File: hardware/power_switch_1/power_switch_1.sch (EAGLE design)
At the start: 21 parts, among them IC1 MEGA168/328, IC2 RFM12, IC3 LP2950Z, K1 FTR-K1C, T1 BC547, X1 SW Out

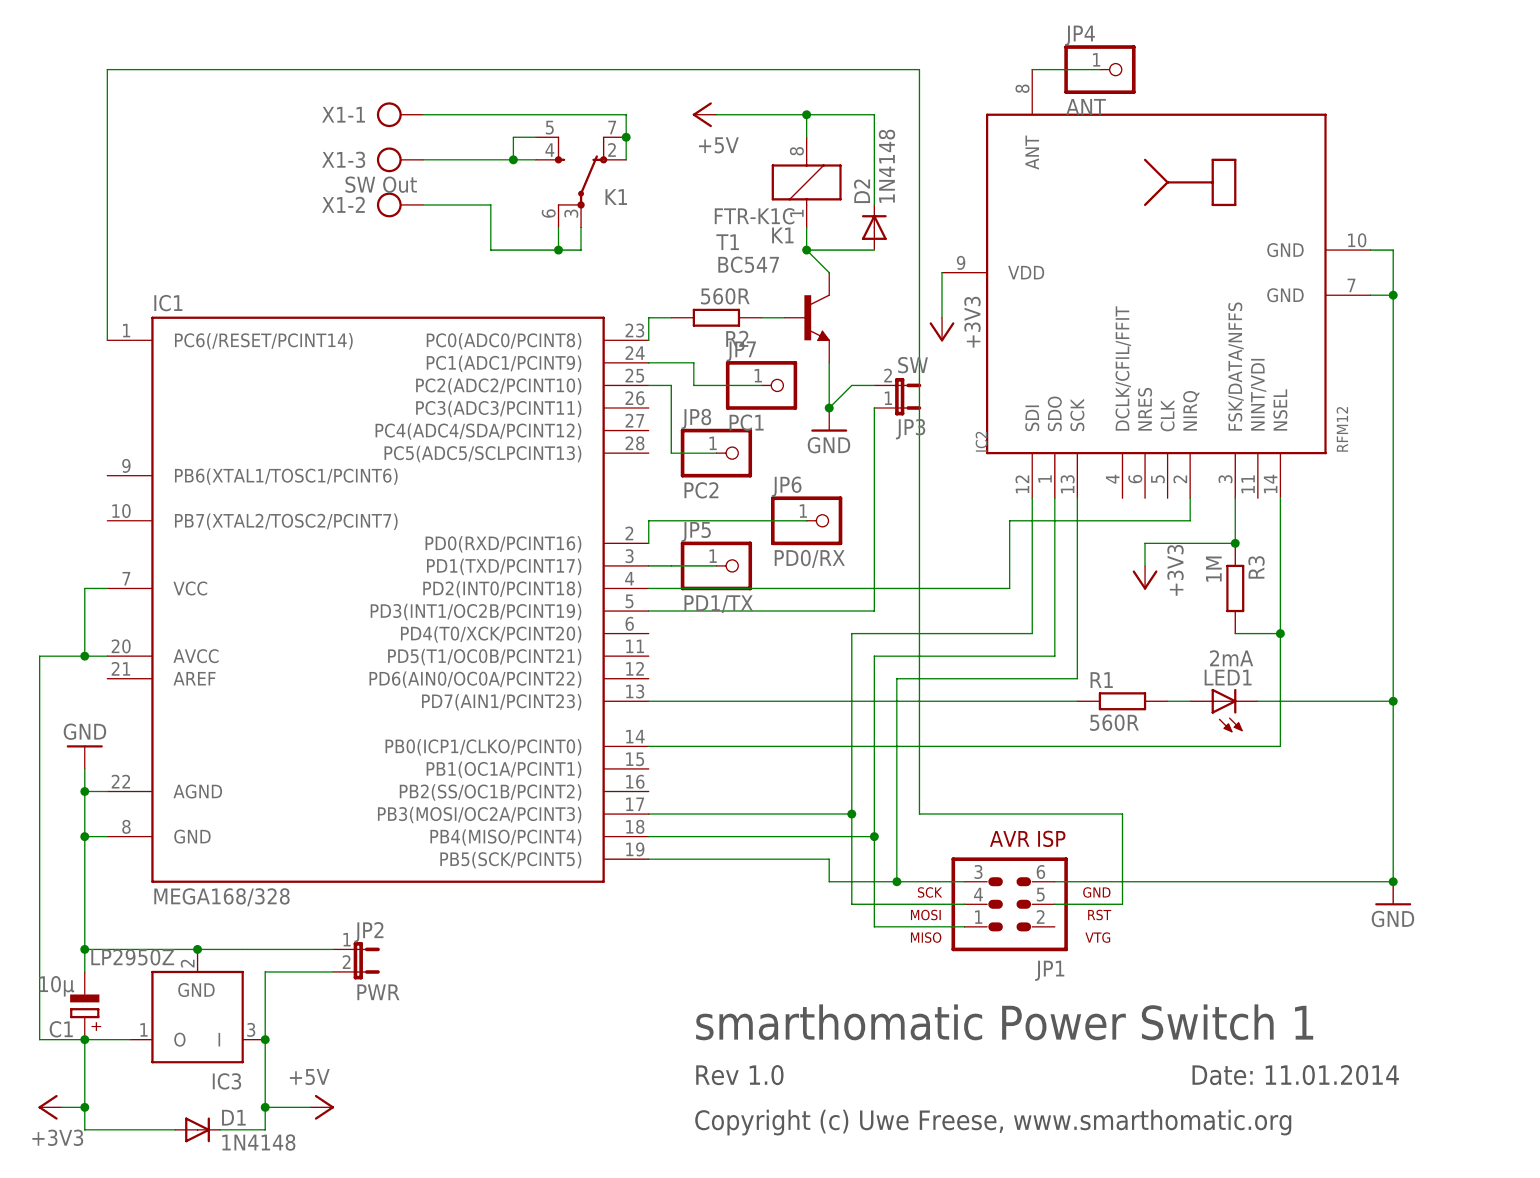
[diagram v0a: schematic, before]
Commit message: In PCB V1.1, the power pin of the RFM module is connected to an ATMega pin to allow restart if needed.
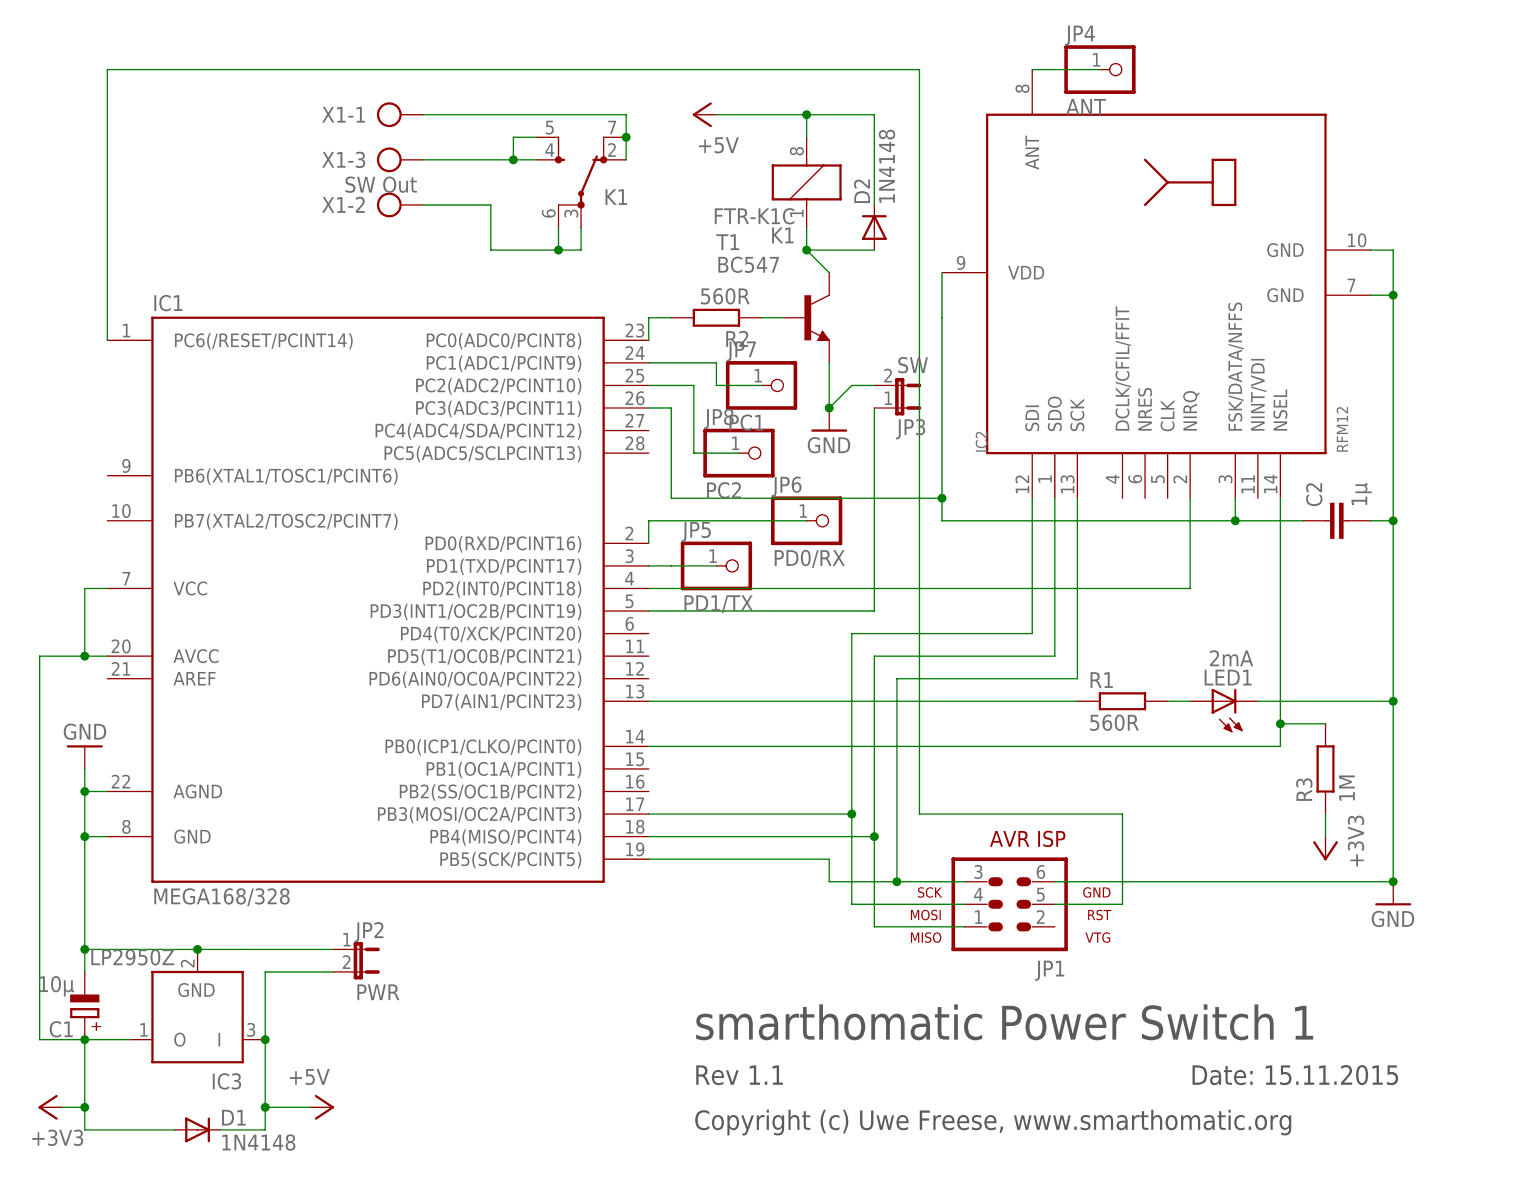
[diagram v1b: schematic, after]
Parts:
- added C2: 1µ, capacitor-wima:C5/3.5
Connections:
- new net N$22: C2.1, IC1.PC3(ADC3/PCINT11), IC2.FSK/DATA/NFFS, IC2.VDD
- net +3V3: no longer IC2.FSK/DATA/NFFS, IC2.VDD
- net GND: now also C2.2
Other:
- note added: "Date: 15.11.2015"
- note added: "Rev 1.1"
- note removed: "Date: 11.01.2014"
- note removed: "Rev 1.0"
- moved on the sheet: JP8, R3
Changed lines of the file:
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@@
 <?xml version="1.0" encoding="utf-8"?>
 <!DOCTYPE eagle SYSTEM "eagle.dtd">
-<eagle version="6.4">
+<eagle version="7.3.0">
 <drawing>
 <settings>
@@
 <part name="P+5" library="supply1" deviceset="+5V" device=""/>
 <part name="T1" library="transistor" deviceset="BC547" device=""/>
-<part name="+3V2" library="supply1" deviceset="+3V3" device=""/>
 <part name="+3V3" library="supply1" deviceset="+3V3" device=""/>
 <part name="K1" library="relay" deviceset="FTR-K1C" device=""/>
@@
 <part name="JP7" library="pinhead" deviceset="PINHD-1X1" device="" value="PC1"/>
 <part name="JP8" library="pinhead" deviceset="PINHD-1X1" device="" value="PC2"/>
+<part name="C2" library="capacitor-wima" deviceset="C" device="5/3.5" value="1µ"/>
 </parts>
 <sheets>
@@
 <frame x1="-48.26" y1="-53.34" x2="132.08" y2="88.9" columns="8" rows="5" layer="97"/>
 <text x="40.64" y="-33.02" size="3.81" layer="97">smarthomatic Power Switch 1</text>
-<text x="96.52" y="-38.1" size="2.1844" layer="97">Date: 11.01.2014</text>
-<text x="40.64" y="-38.1" size="2.1844" layer="97">Rev 1.0</text>
+<text x="96.52" y="-38.1" size="2.1844" layer="97">Date: 15.11.2015</text>
+<text x="40.64" y="-38.1" size="2.1844" layer="97">Rev 1.1</text>
 <text x="40.64" y="-43.18" size="2.1844" layer="97">Copyright (c) Uwe Freese, www.smarthomatic.org</text>
 </plain>
@@
 <instance part="C1" gate="G$1" x="-27.94" y="-30.48" rot="R180"/>
 <instance part="GND3" gate="1" x="55.88" y="35.56"/>
-<instance part="R3" gate="G$1" x="101.6" y="17.78" rot="R270"/>
+<instance part="R3" gate="G$1" x="111.76" y="-2.54" rot="R90"/>
 <instance part="JP2" gate="A" x="2.54" y="-22.86" rot="R270"/>
 <instance part="JP4" gate="G$1" x="88.9" y="76.2"/>
@@
 <instance part="P+5" gate="1" x="0" y="-40.64" rot="R270"/>
 <instance part="T1" gate="G$1" x="53.34" y="48.26"/>
-<instance part="+3V2" gate="G$1" x="68.58" y="45.72" rot="R180"/>
-<instance part="+3V3" gate="G$1" x="91.44" y="17.78" rot="R180"/>
+<instance part="+3V3" gate="G$1" x="111.76" y="-12.7" rot="R180"/>
 <instance part="K1" gate="-1" x="27.94" y="60.96"/>
 <instance part="K1" gate="K" x="53.34" y="63.5" rot="R180"/>
@@
 <instance part="JP6" gate="G$1" x="55.88" y="25.4"/>
 <instance part="JP7" gate="G$1" x="50.8" y="40.64"/>
-<instance part="JP8" gate="G$1" x="45.72" y="33.02"/>
+<instance part="JP8" gate="G$1" x="48.26" y="33.02"/>
+<instance part="C2" gate="G$1" x="111.76" y="25.4" rot="R90"/>
 </instances>
 <busses>
@@
 <wire x1="81.28" y1="-15.24" x2="119.38" y2="-15.24" width="0.1524" layer="91"/>
 <pinref part="GND2" gate="1" pin="GND"/>
-<wire x1="119.38" y1="50.8" x2="119.38" y2="5.08" width="0.1524" layer="91"/>
+<wire x1="119.38" y1="50.8" x2="119.38" y2="25.4" width="0.1524" layer="91"/>
 <junction x="119.38" y="-15.24"/>
 <pinref part="LED1" gate="G$1" pin="C"/>
+<wire x1="119.38" y1="25.4" x2="119.38" y2="5.08" width="0.1524" layer="91"/>
 <wire x1="119.38" y1="5.08" x2="119.38" y2="-15.24" width="0.1524" layer="91"/>
 <wire x1="104.14" y1="5.08" x2="119.38" y2="5.08" width="0.1524" layer="91"/>
@@
 <wire x1="119.38" y1="55.88" x2="119.38" y2="50.8" width="0.1524" layer="91"/>
 <junction x="119.38" y="50.8"/>
+<pinref part="C2" gate="G$1" pin="2"/>
+<wire x1="116.84" y1="25.4" x2="119.38" y2="25.4" width="0.1524" layer="91"/>
+<junction x="119.38" y="25.4"/>
 </segment>
 <segment>
@@
 <segment>
 <pinref part="IC2" gate="G$1" pin="NSEL"/>
-<wire x1="101.6" y1="12.7" x2="106.68" y2="12.7" width="0.1524" layer="91"/>
+<wire x1="111.76" y1="2.54" x2="106.68" y2="2.54" width="0.1524" layer="91"/>
 <pinref part="R3" gate="G$1" pin="2"/>
 <pinref part="IC1" gate="1" pin="PB0(ICP1/CLKO/PCINT0)"/>
-<wire x1="106.68" y1="12.7" x2="106.68" y2="27.94" width="0.1524" layer="91"/>
+<wire x1="106.68" y1="2.54" x2="106.68" y2="27.94" width="0.1524" layer="91"/>
 <wire x1="35.56" y1="0" x2="106.68" y2="0" width="0.1524" layer="91"/>
-<wire x1="106.68" y1="0" x2="106.68" y2="12.7" width="0.1524" layer="91"/>
-<junction x="106.68" y="12.7"/>
+<wire x1="106.68" y1="0" x2="106.68" y2="2.54" width="0.1524" layer="91"/>
+<junction x="106.68" y="2.54"/>
 </segment>
 </net>
@@
 <pinref part="IC1" gate="1" pin="PD2(INT0/PCINT18)"/>
 <wire x1="35.56" y1="17.78" x2="76.2" y2="17.78" width="0.1524" layer="91"/>
-<wire x1="76.2" y1="17.78" x2="76.2" y2="25.4" width="0.1524" layer="91"/>
-<wire x1="76.2" y1="25.4" x2="96.52" y2="25.4" width="0.1524" layer="91"/>
+<wire x1="76.2" y1="17.78" x2="96.52" y2="17.78" width="0.1524" layer="91"/>
 <pinref part="IC2" gate="G$1" pin="NIRQ"/>
-<wire x1="96.52" y1="25.4" x2="96.52" y2="27.94" width="0.1524" layer="91"/>
+<wire x1="96.52" y1="17.78" x2="96.52" y2="27.94" width="0.1524" layer="91"/>
 </segment>
 </net>
@@
 </segment>
 <segment>
-<pinref part="IC2" gate="G$1" pin="VDD"/>
-<wire x1="68.58" y1="53.34" x2="68.58" y2="48.26" width="0.1524" layer="91"/>
-<pinref part="+3V2" gate="G$1" pin="+3V3"/>
-</segment>
-<segment>
-<wire x1="101.6" y1="22.86" x2="91.44" y2="22.86" width="0.1524" layer="91"/>
-<wire x1="91.44" y1="22.86" x2="91.44" y2="20.32" width="0.1524" layer="91"/>
-<junction x="101.6" y="22.86"/>
-<pinref part="IC2" gate="G$1" pin="FSK/DATA/NFFS"/>
-<wire x1="101.6" y1="27.94" x2="101.6" y2="22.86" width="0.1524" layer="91"/>
+<wire x1="111.76" y1="-7.62" x2="111.76" y2="-10.16" width="0.1524" layer="91"/>
 <pinref part="R3" gate="G$1" pin="1"/>
 <pinref part="+3V3" gate="G$1" pin="+3V3"/>
@@
 <pinref part="IC1" gate="1" pin="PC1(ADC1/PCINT9)"/>
 <pinref part="JP7" gate="G$1" pin="1"/>
-<wire x1="35.56" y1="43.18" x2="40.64" y2="43.18" width="0.1524" layer="91"/>
-<wire x1="40.64" y1="43.18" x2="40.64" y2="40.64" width="0.1524" layer="91"/>
-<wire x1="40.64" y1="40.64" x2="48.26" y2="40.64" width="0.1524" layer="91"/>
+<wire x1="35.56" y1="43.18" x2="43.18" y2="43.18" width="0.1524" layer="91"/>
+<wire x1="43.18" y1="43.18" x2="43.18" y2="40.64" width="0.1524" layer="91"/>
+<wire x1="43.18" y1="40.64" x2="48.26" y2="40.64" width="0.1524" layer="91"/>
 </segment>
 </net>
@@
 <pinref part="IC1" gate="1" pin="PC2(ADC2/PCINT10)"/>
 <pinref part="JP8" gate="G$1" pin="1"/>
-<wire x1="35.56" y1="40.64" x2="38.1" y2="40.64" width="0.1524" layer="91"/>
-<wire x1="38.1" y1="40.64" x2="38.1" y2="33.02" width="0.1524" layer="91"/>
-<wire x1="38.1" y1="33.02" x2="43.18" y2="33.02" width="0.1524" layer="91"/>
+<wire x1="35.56" y1="40.64" x2="40.64" y2="40.64" width="0.1524" layer="91"/>
+<wire x1="40.64" y1="40.64" x2="40.64" y2="33.02" width="0.1524" layer="91"/>
+<wire x1="40.64" y1="33.02" x2="45.72" y2="33.02" width="0.1524" layer="91"/>
 </segment>
 </net>
@@
 </segment>
 </net>
+<net name="N$22" class="0">
+<segment>
+<pinref part="IC2" gate="G$1" pin="VDD"/>
+<wire x1="68.58" y1="53.34" x2="68.58" y2="48.26" width="0.1524" layer="91"/>
+<wire x1="68.58" y1="48.26" x2="68.58" y2="27.94" width="0.1524" layer="91"/>
+<wire x1="68.58" y1="27.94" x2="38.1" y2="27.94" width="0.1524" layer="91"/>
+<wire x1="38.1" y1="27.94" x2="38.1" y2="38.1" width="0.1524" layer="91"/>
+<pinref part="IC1" gate="1" pin="PC3(ADC3/PCINT11)"/>
+<wire x1="38.1" y1="38.1" x2="35.56" y2="38.1" width="0.1524" layer="91"/>
+<pinref part="IC2" gate="G$1" pin="FSK/DATA/NFFS"/>
+<wire x1="101.6" y1="27.94" x2="101.6" y2="25.4" width="0.1524" layer="91"/>
+<wire x1="101.6" y1="25.4" x2="68.58" y2="25.4" width="0.1524" layer="91"/>
+<wire x1="68.58" y1="25.4" x2="68.58" y2="27.94" width="0.1524" layer="91"/>
+<junction x="68.58" y="27.94"/>
+<pinref part="C2" gate="G$1" pin="1"/>
+<wire x1="101.6" y1="25.4" x2="109.22" y2="25.4" width="0.1524" layer="91"/>
+<junction x="101.6" y="25.4"/>
+</segment>
+</net>
